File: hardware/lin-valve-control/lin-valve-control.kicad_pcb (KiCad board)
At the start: 4 copper layers, 78.2 x 43.2 mm, 29 parts, among them J1 QWIIC Connector, J2 DIN-5_180degree, J3 DIN-5_180degree, J4 Screw_Terminal_01x02, J5 Screw_Terminal_01x03, J6 Screw_Terminal_01x03, Q1 2N7002, Q2 2N7002, U1 Arduino_Nano_v3.x, U2 TJA1021T, U3 DRV8833PWP

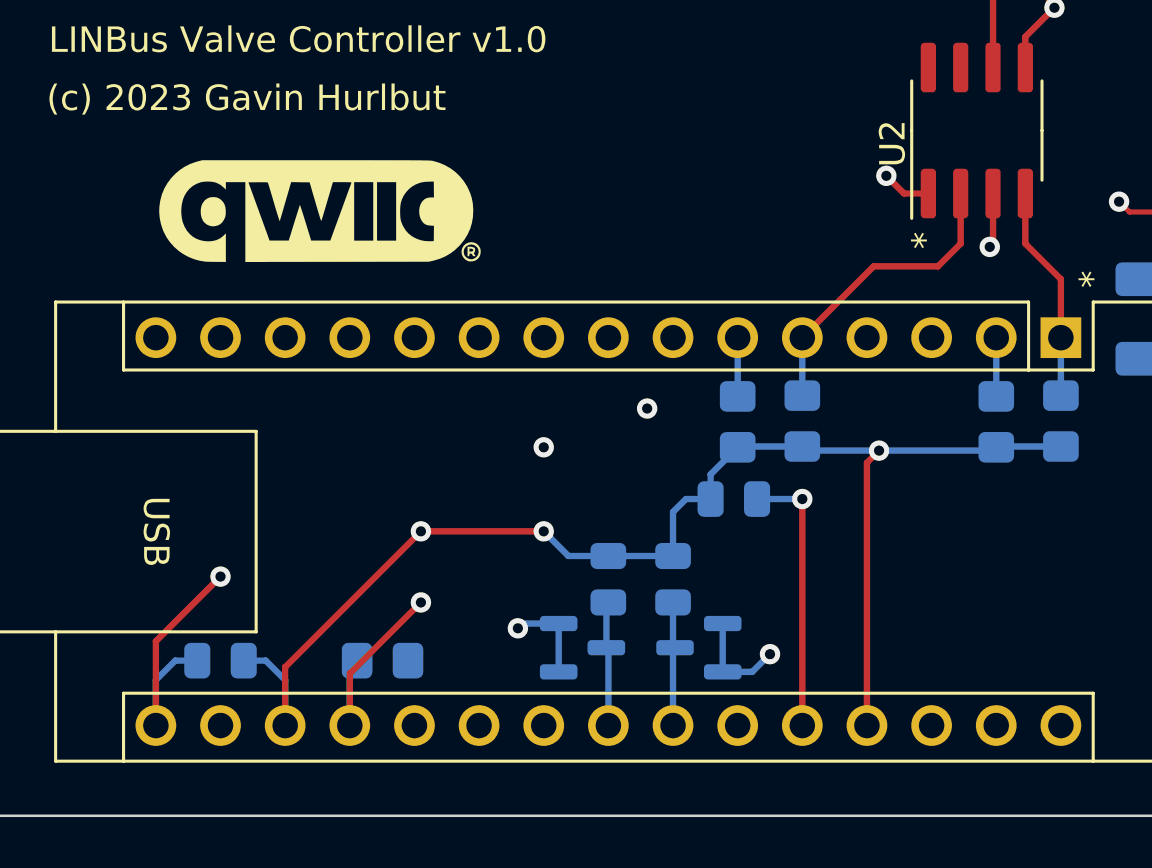
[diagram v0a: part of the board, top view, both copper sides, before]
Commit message: Added firmware v1 for the valve-control board
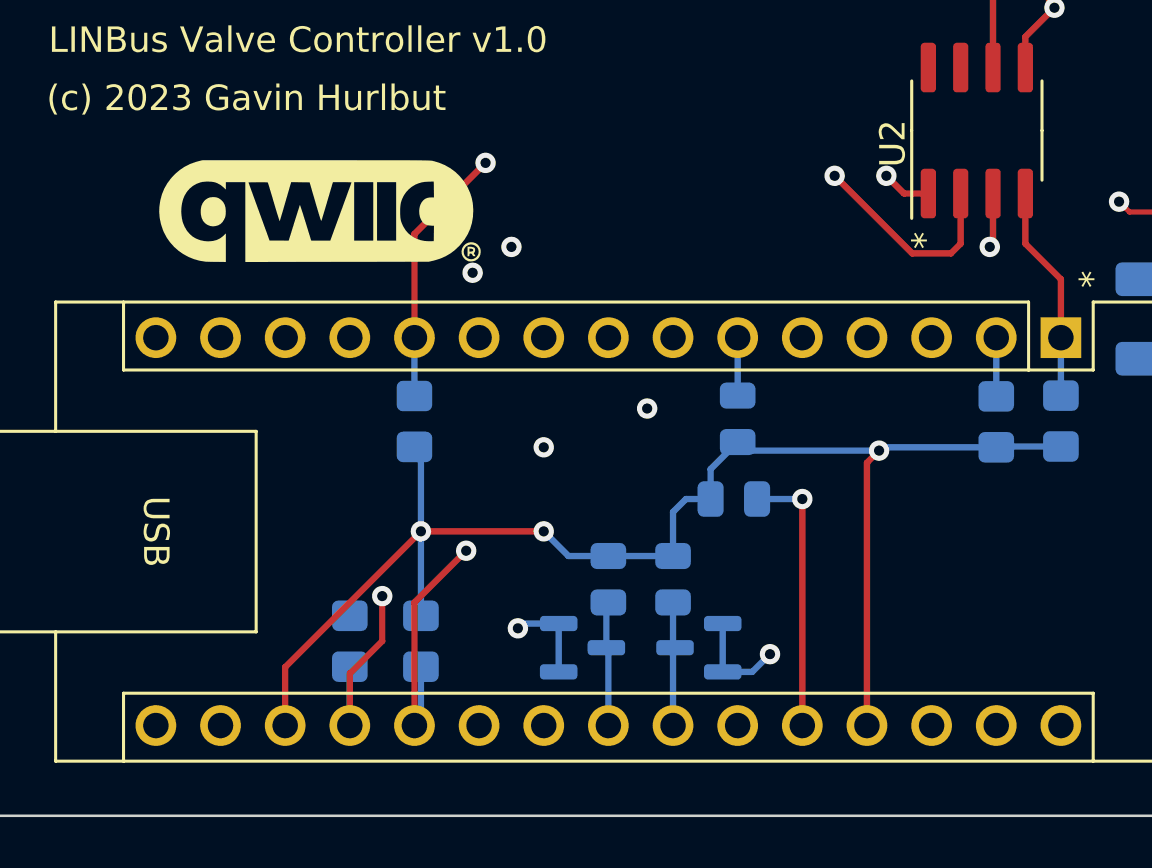
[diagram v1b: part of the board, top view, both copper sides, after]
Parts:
- moved R9 22.4 mm to (182.1, 86.0), turned to 90 degrees
- moved R4 15.2 mm to (169.4, 86.1)
- moved R6 15.1 mm to (169.7, 94.7), turned to -90 degrees
- moved R3 1.49 mm to (166.9, 94.7), turned to 90 degrees
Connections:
- U1 pad 11: FLOW_PULSE -> ~{LIN_SLP}
- U1 pad 16: ~{MOTOR_FAULT} -> unconnected-(U1-Pad16)
- U1 pad 20: unconnected-(U1-Pad20) -> ~{LIN_WAKE}
- U1 pad 5: ~{LIN_SLP} -> FLOW_PULSE
- U1 pad 6: ~{LIN_WAKE} -> ~{MOTOR_FAULT}
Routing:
- net ~{MOTOR_FAULT}: track 68.5 -> 37.8 mm, vias 2 -> 1
- net ~{LIN_WAKE}: track 17.3 -> 43.7 mm, vias 1 -> 3
- net ~{LIN_SLP}: track 12.0 -> 32.6 mm, vias 0 -> 2
- net FLOW_PULSE: track 22.1 -> 34.8 mm, vias 1 -> 2
- net +5V: track 85.6 -> 89.1 mm
- net MOTOR_EN: track 54.8 -> 56.0 mm

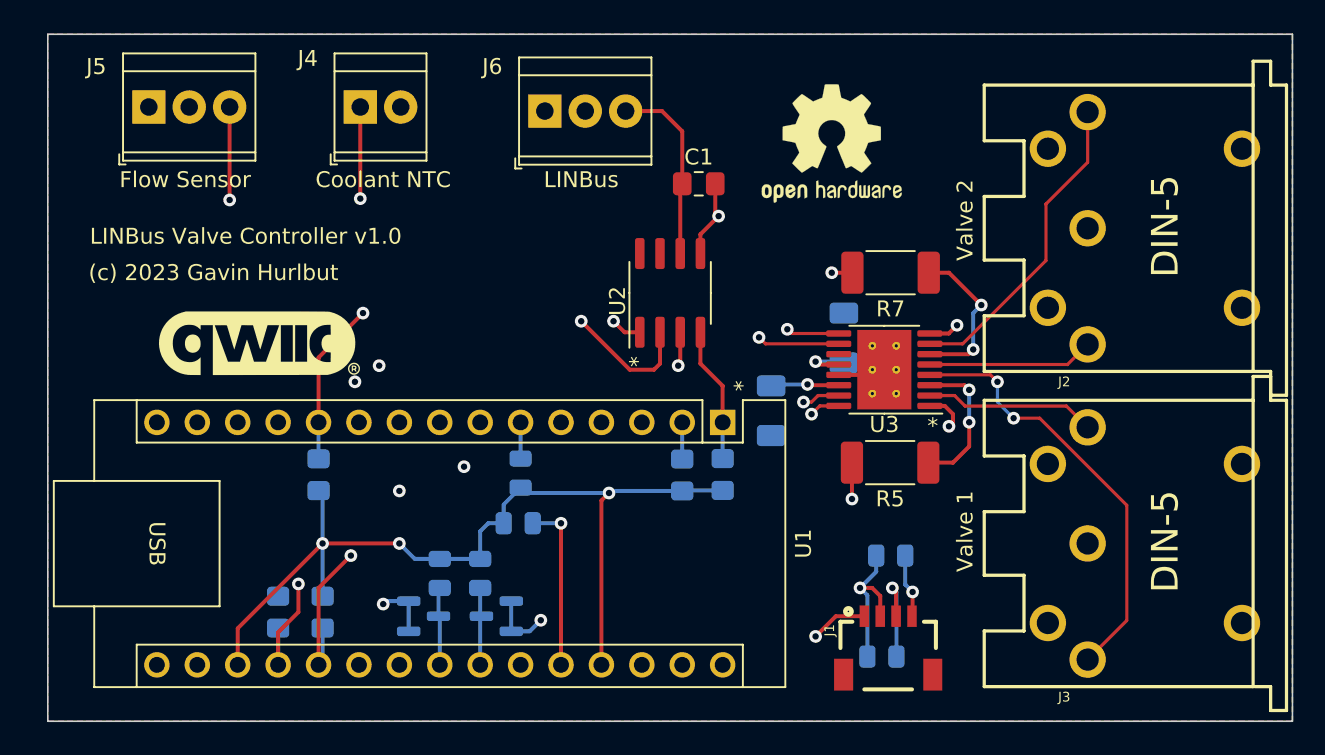
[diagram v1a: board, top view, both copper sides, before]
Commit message: Put in the Coolant Pump and Cooling Fan bits
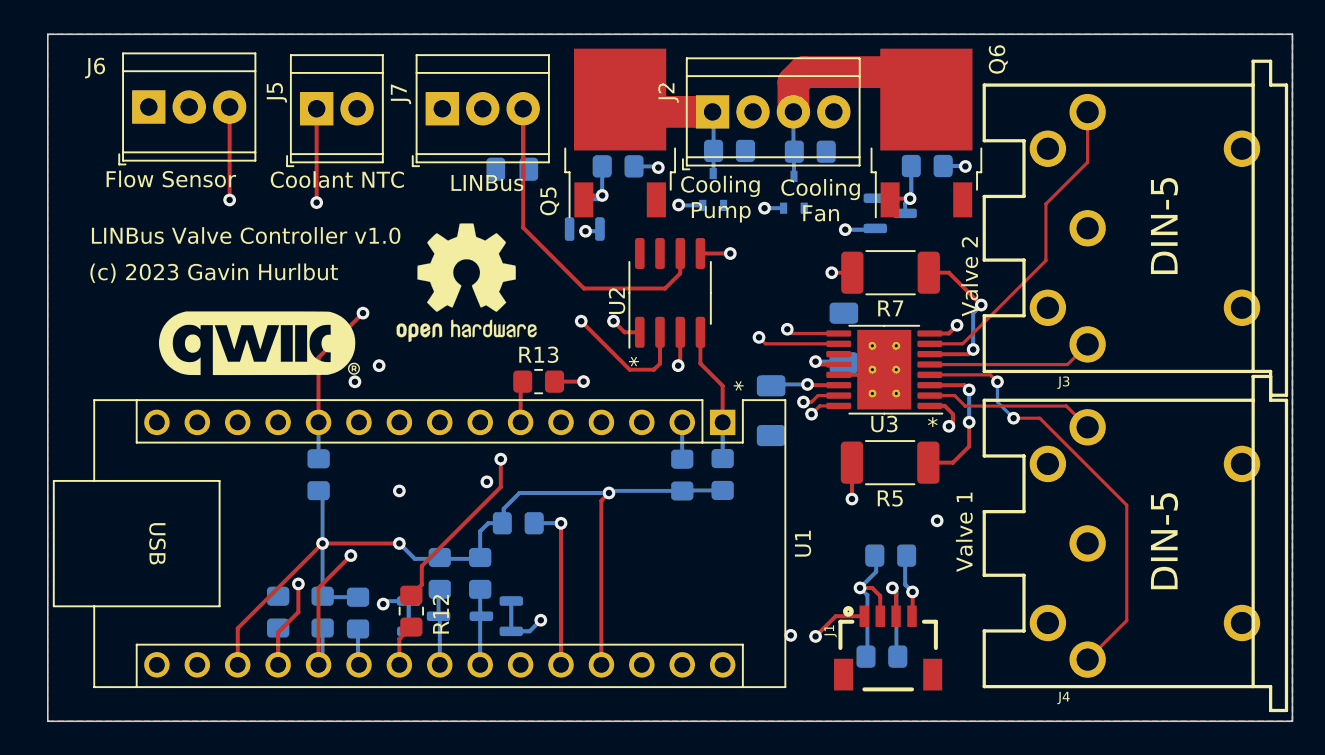
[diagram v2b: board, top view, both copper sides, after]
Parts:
- added D1: BAT54SW, Package_TO_SOT_SMD:SOT-323_SC-70, B.Cu at (194.2, 68.2)
- added D2: BAT54SW, Package_TO_SOT_SMD:SOT-323_SC-70, B.Cu at (199.3, 68.3)
- added J2: Screw_Terminal_01x04, TerminalBlock_TE-Connectivity:TerminalBlock_TE_282834-4_1x04_P2.54mm_Horizontal, F.Cu at (194.2, 63.3)
- added Q3: 2N7002, Package_TO_SOT_SMD:SOT-23, B.Cu at (186.2, 69.7)
- added Q4: 2N7002, Package_TO_SOT_SMD:SOT-23, B.Cu at (205.3, 69.7)
- added Q5: SUD50P04-08, Package_TO_SOT_SMD:TO-252-2, F.Cu at (188.4, 64.6)
- added Q6: SUD50P04-08, Package_TO_SOT_SMD:TO-252-2, F.Cu at (207.6, 64.6)
- added R12: 10R, Resistor_SMD:R_0805_2012Metric_Pad1.20x1.40mm_HandSolder, F.Cu at (175.2, 94.7)
- added R13: 10R, Resistor_SMD:R_0805_2012Metric_Pad1.20x1.40mm_HandSolder, F.Cu at (183.2, 80.2)
- added R14: 10k, Resistor_SMD:R_0805_2012Metric_Pad1.20x1.40mm_HandSolder, B.Cu at (188.2, 66.7)
- added R16: 10k, Resistor_SMD:R_0805_2012Metric_Pad1.20x1.40mm_HandSolder, B.Cu at (207.7, 66.7)
- added R18: 10R, Resistor_SMD:R_0805_2012Metric_Pad1.20x1.40mm_HandSolder, B.Cu at (195.2, 65.8)
- added R19: 10R, Resistor_SMD:R_0805_2012Metric_Pad1.20x1.40mm_HandSolder, B.Cu at (200.3, 65.8)
- C1: moved to B.Cu
- R10, R11, R8, R9: footprint Resistor_SMD:R_0805_2012Metric -> Resistor_SMD:R_0805_2012Metric_Pad1.20x1.40mm_HandSolder
- R15: renamed from R12; footprint Resistor_SMD:R_0805_2012Metric -> Resistor_SMD:R_0805_2012Metric_Pad1.20x1.40mm_HandSolder
- R17: renamed from R13; footprint Resistor_SMD:R_0805_2012Metric -> Resistor_SMD:R_0805_2012Metric_Pad1.20x1.40mm_HandSolder
- moved REF** 24.6 mm to (178.7, 74.0)
- moved R9 13.5 mm to (171.9, 94.8), turned to -90 degrees
- moved C1 11.8 mm to (181.6, 66.9), turned to 180 degrees
- moved J7 6.44 mm to (177.2, 63.1)
- moved J5 2.74 mm to (169.3, 63.1)
- renumbered J2 to J3, J3 to J4, J4 to J5, J5 to J6, J6 to J7
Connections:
- U1 pad 21: unconnected-(U1-Pad21) -> ~{MOTOR_FAULT}
- U1 pad 22: unconnected-(U1-Pad22) -> PUMP_EN
- U1 pad 6: ~{MOTOR_FAULT} -> FAN_PWM
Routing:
- net Net-(Q3-Pad1): track 0.00 -> 28.4 mm, vias 0 -> 2
- net Net-(Q4-Pad1): track 0.00 -> 27.8 mm, vias 0 -> 2
- net ~{MOTOR_FAULT}: track 37.8 -> 59.9 mm, vias 1 -> 3
- net COOLING_FAN: track 0.00 -> 15.3 mm
- net LIN: track 11.8 -> 24.5 mm
- net COOLANT_PUMP: track 0.00 -> 10.1 mm
- net +12V: track 3.34 -> 9.04 mm, vias 1 -> 5
- net Net-(Q4-Pad3): track 0.00 -> 4.42 mm, vias 0 -> 1
- net Net-(Q3-Pad3): track 0.00 -> 4.29 mm, vias 0 -> 1
- net GND: track 14.6 -> 11.6 mm
- net COOLANT_NTC: track 42.1 -> 44.9 mm
- net PUMP_EN: track 0.00 -> 2.69 mm
- net FAN_PWM: track 0.00 -> 2.62 mm
- net +5V: track 89.1 -> 90.8 mm
- net VALVE_IN1+: track 29.1 -> 28.0 mm
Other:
- board text added: "Cooling Fan"
- board text added: "Cooling Pump"

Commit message: Update lin-master firmware and valve control board
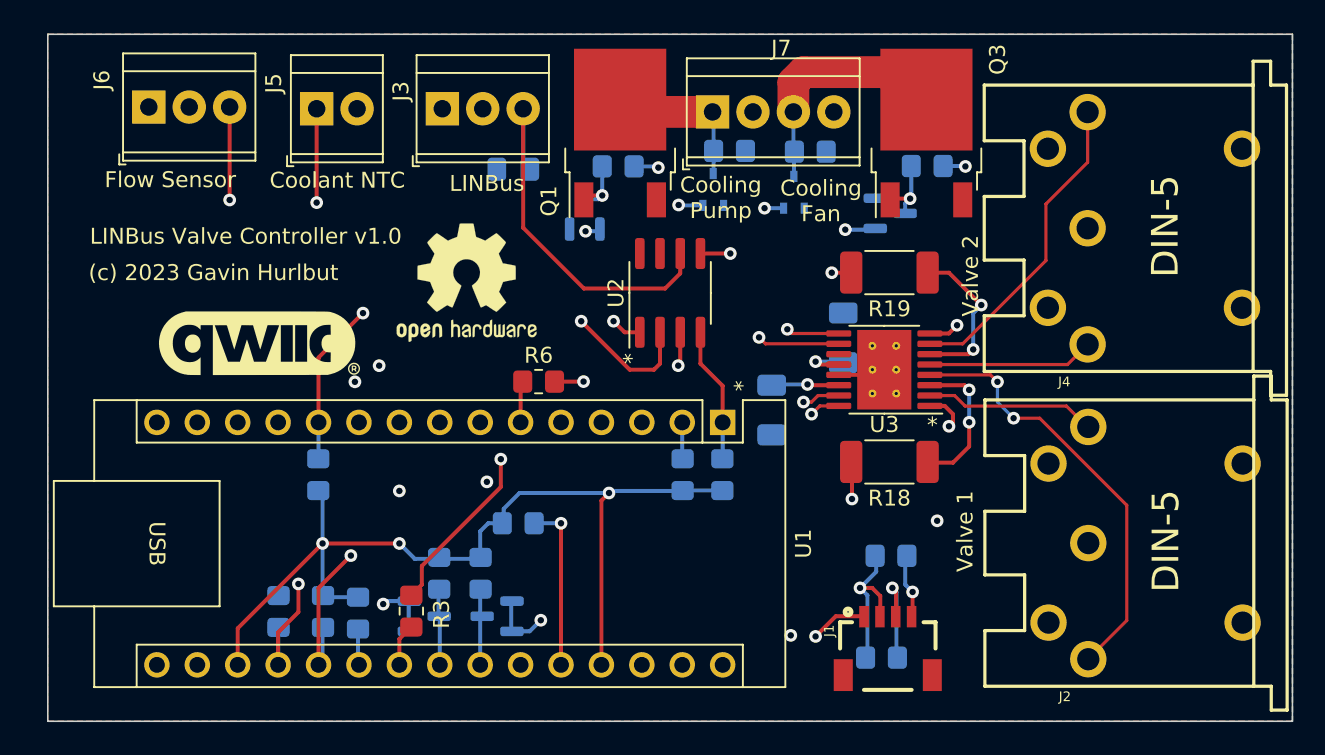
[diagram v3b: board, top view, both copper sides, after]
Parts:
- removed the Q1 at (180.6, 95.0)
- removed the Q2 at (176.0, 95.0)
- removed the R1 at (192.3, 86.1)
- removed the R2 at (194.8, 86.1)
- removed the R3 at (166.9, 94.7)
- removed the R4 at (169.4, 86.1)
- removed the R5 at (205.3, 85.3)
- removed the R6 at (169.7, 94.7)
- removed the R7 at (205.4, 73.4)
- added Q5: 2N7002, Package_TO_SOT_SMD:SOT-23, B.Cu at (176.1, 95.0)
- added Q6: 2N7002, Package_TO_SOT_SMD:SOT-23, B.Cu at (180.6, 95.0)
- added R12: 10k, Resistor_SMD:R_0805_2012Metric_Pad1.20x1.40mm_HandSolder, B.Cu at (192.3, 86.1)
- added R13: 10k, Resistor_SMD:R_0805_2012Metric_Pad1.20x1.40mm_HandSolder, B.Cu at (194.8, 86.1)
- added R14: 10k, Resistor_SMD:R_0805_2012Metric_Pad1.20x1.40mm_HandSolder, B.Cu at (169.4, 86.1)
- added R16: 10k, Resistor_SMD:R_0805_2012Metric_Pad1.20x1.40mm_HandSolder, B.Cu at (171.9, 94.8)
- added R18: 2R 2W, Resistor_SMD:R_2010_5025Metric_Pad1.40x2.65mm_HandSolder, F.Cu at (205.3, 85.3)
- added R19: 2R 2W, Resistor_SMD:R_2010_5025Metric_Pad1.40x2.65mm_HandSolder, F.Cu at (205.3, 73.4)
- added R8: 10k, Resistor_SMD:R_0805_2012Metric_Pad1.20x1.40mm_HandSolder, B.Cu at (179.6, 92.3)
- J2: value Screw_Terminal_01x04 -> DIN5; footprint TerminalBlock_TE-Connectivity:TerminalBlock_TE_282834-4_1x04_P2.54mm_Horizontal -> SparkFun-Connectors:DIN5-RA-PTH
- J3: value DIN-5_180degree -> Screw_Terminal_01x03; footprint SparkFun-Connectors:DIN5-RA-PTH -> TerminalBlock_TE-Connectivity:TerminalBlock_TE_282834-3_1x03_P2.54mm_Horizontal
- J4: value DIN-5_180degree -> DIN5
- J7: value Screw_Terminal_01x03 -> Screw_Terminal_01x04; footprint TerminalBlock_TE-Connectivity:TerminalBlock_TE_282834-3_1x03_P2.54mm_Horizontal -> TerminalBlock_TE-Connectivity:TerminalBlock_TE_282834-4_1x04_P2.54mm_Horizontal
- moved J3 53.6 mm to (177.2, 63.1), turned to 0 degrees
- moved J2 45.2 mm to (230.3, 90.4), turned to 90 degrees
- moved R17 38.6 mm to (166.9, 94.7), turned to 90 degrees
- moved R15 35.2 mm to (169.7, 94.7), turned to -90 degrees
- moved R9 33.0 mm to (204.8, 97.6), turned to 0 degrees
- moved R10 28.4 mm to (205.4, 91.2), turned to 0 degrees
- moved J4 19.8 mm to (230.3, 70.6)
- moved J7 17.0 mm to (194.2, 63.3)
- moved R11 2.58 mm to (177.0, 92.3)
- moved C1 0.06 mm to (181.7, 66.9)
- moved C3 0.05 mm to (197.9, 82.0)
- renumbered Q5 to Q1, Q3 to Q2, Q6 to Q3, R8 to R1, R14 to R2, R12 to R3, R18 to R4, R16 to R5, R13 to R6, R19 to R7
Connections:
- J2 pad 1: COOLANT_PUMP -> VALVE1+
- J2 pad 3: COOLING_FAN -> VALVE1-
- J2 pad 4: GND -> VALVE1_OPEN
- J3 pad 1: VALVE2+ -> +12V
- J3 pad 3: VALVE2- -> LIN
- J4 pad 1: VALVE1+ -> VALVE2+
- J4 pad 3: VALVE1- -> VALVE2-
- J4 pad 4: VALVE1_OPEN -> VALVE2_OPEN
- J4 pad 5: VALVE1_CLOSED -> VALVE2_CLOSED
- J7 pad 1: +12V -> COOLANT_PUMP
- J7 pad 3: LIN -> COOLING_FAN
- R10 pad 1: +5V -> +3V3
- R10 pad 2: SDA5 -> SCL
- R11 pad 2: SCL5 -> SDA5
- R15 pad 1: +3V3 -> +5V
- R15 pad 2: SDA -> ~{LIN_WAKE}
- R17 pad 1: +3V3 -> MOTOR_EN
- R17 pad 2: SCL -> GND
- R9 pad 1: +5V -> +3V3
- R9 pad 2: ~{MOTOR_FAULT} -> SDA

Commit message: Updated valve controller board
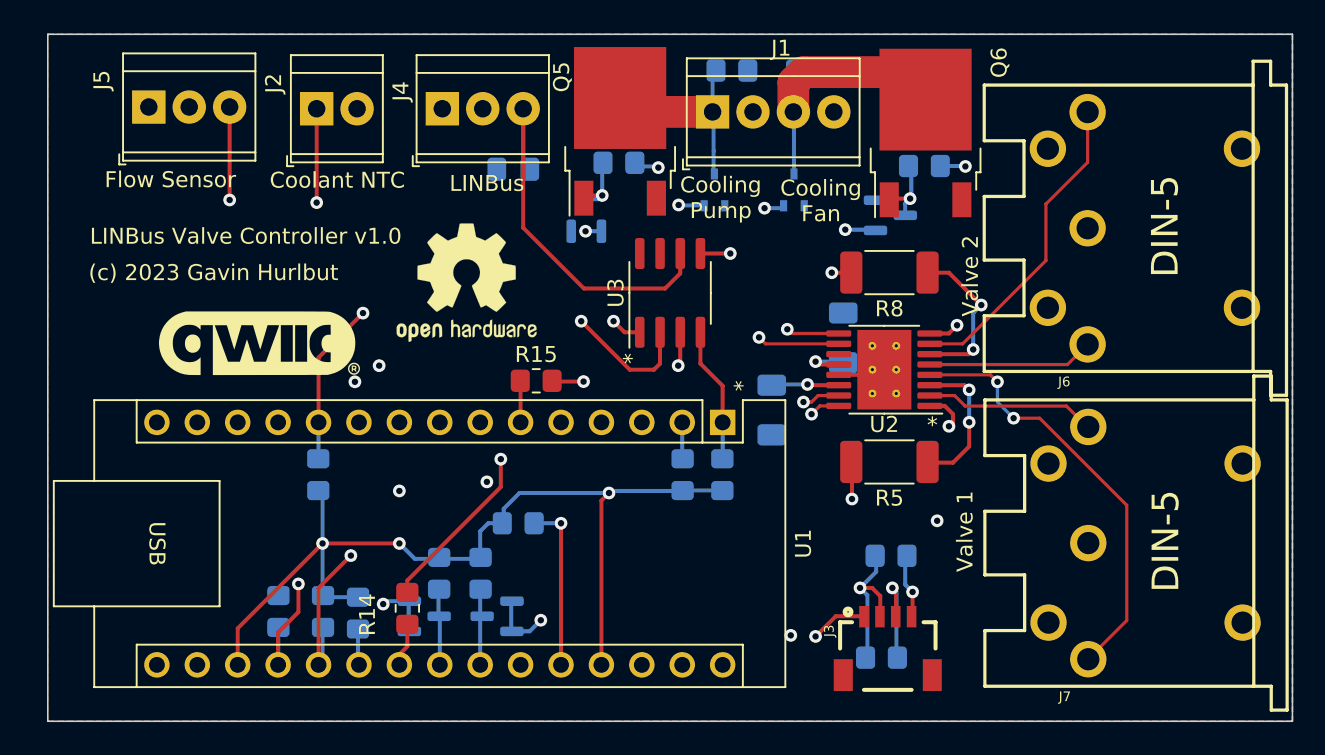
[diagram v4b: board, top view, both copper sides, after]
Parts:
- removed the Q1 at (188.4, 64.6)
- removed the Q2 at (186.2, 69.7)
- removed the R2 at (188.2, 66.7)
- removed the R3 at (175.2, 94.7)
- removed the R4 at (195.2, 65.8)
- removed the R5 at (207.7, 66.7)
- removed the R6 at (183.2, 80.2)
- removed the R7 at (200.3, 65.8)
- added Q5: SUD50P04-08, Package_TO_SOT_SMD:TO-252-2, F.Cu at (188.4, 64.5)
- added Q6: SUD50P04-08, Package_TO_SOT_SMD:TO-252-2, F.Cu at (207.6, 64.6)
- added R14: 10R, Resistor_SMD:R_0805_2012Metric_Pad1.20x1.40mm_HandSolder, F.Cu at (175.0, 94.5)
- added R15: 10R, Resistor_SMD:R_0805_2012Metric_Pad1.20x1.40mm_HandSolder, F.Cu at (183.1, 80.2)
- added R16: 10k, Resistor_SMD:R_0805_2012Metric_Pad1.20x1.40mm_HandSolder, B.Cu at (188.3, 66.5)
- added R17: 10k, Resistor_SMD:R_0805_2012Metric_Pad1.20x1.40mm_HandSolder, B.Cu at (207.5, 66.7)
- added R18: 10R, Resistor_SMD:R_0805_2012Metric_Pad1.20x1.40mm_HandSolder, B.Cu at (195.4, 60.7)
- added R19: 10R, Resistor_SMD:R_0805_2012Metric_Pad1.20x1.40mm_HandSolder, B.Cu at (200.4, 60.7)
- Q3: value SUD50P04-08 -> 2N7002; footprint Package_TO_SOT_SMD:TO-252-2 -> Package_TO_SOT_SMD:SOT-23; moved to B.Cu
- moved Q3 22.0 mm to (186.2, 69.9)
- moved D2 0.15 mm to (199.3, 68.2)
- moved Q4 0.13 mm to (205.4, 69.8)
- moved D1 0.08 mm to (194.3, 68.2)
- renumbered C2 to C1, C1 to C2, J7 to J1, J5 to J2, J1 to J3, J3 to J4, J6 to J5, J4 to J6, J2 to J7, Q6 to Q1, Q5 to Q2, R15 to R10, R9 to R11, R16 to R12, R10 to R13, R12 to R2, R17 to R3, R11 to R4, R18 to R5, R13 to R6, R8 to R7, R19 to R8, R14 to R9, U3 to U2, U2 to U3
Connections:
- net SCL renamed SCL3V
- net SCL5 renamed SCL5V
- net SDA renamed SDA3V
- net SDA5 renamed SDA5V
- Q3 pad 2: COOLING_FAN -> GND
- Q3 pad 3: +12V -> Net-(Q3-Pad3)
- Q4 pad 3: Net-(Q3-Pad1) -> Net-(Q4-Pad3)
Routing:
- net Net-(Q2-Pad1): track 28.4 -> 0.00 mm, vias 2 -> 0
- net Net-(Q3-Pad1): track 4.42 -> 28.3 mm, vias 1 -> 2
- net Net-(Q4-Pad3): track 0.00 -> 4.42 mm, vias 0 -> 1
- net Net-(Q3-Pad3): track 0.00 -> 4.29 mm, vias 0 -> 1
- net Net-(Q1-Pad1): track 4.29 -> 0.00 mm, vias 1 -> 0
- net COOLANT_PUMP: track 10.1 -> 12.7 mm
- net COOLING_FAN: track 15.3 -> 17.8 mm
